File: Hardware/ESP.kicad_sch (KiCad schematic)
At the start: 30 parts, among them J2 USB_C_Receptacle_USB2.0_16P, SW1 RESET, SW2 BOOT, U1 ESP32-C6-MINI-1/U, U2 TPS2115ADRBR, U8 LT1963AEST-3.3#TRPBF

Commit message: revB updates
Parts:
- removed C18: 0.1u, Capacitor_SMD:C_0603_1608Metric, symbol Device:C
- removed R15, R22, R23: 10k, Resistor_SMD:R_0603_1608Metric, symbol Device:R_US
- removed SW1: RESET, UTSVT_Special:SW_SPST_B3SL-1002P, symbol Switch:SW_MEC_5G
- removed SW2: BOOT, UTSVT_Special:SW_CJS-1200TA, symbol Switch:SW_SPDT
- added R1: 10k, Resistor_SMD:R_0603_1608Metric, symbol Device:R_US
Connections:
- net BOOT_SWITCH is gone; now on net BOOT: U1.23 (GPIO9)
- net +3.3V_ESP: now also R7.1, TP47.1, R1.1
- net +3.3V_USB: no longer R7.1, TP47.1
- net BOOT: no longer U1.22 (GPIO8)
- new net: R1.2, U1.22 (GPIO8)

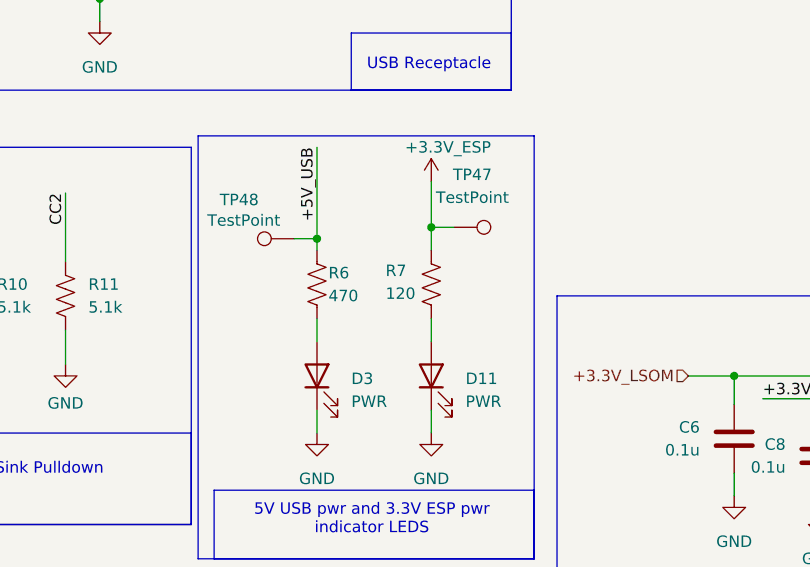
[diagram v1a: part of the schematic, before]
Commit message: Schematic polishes, layout WIP
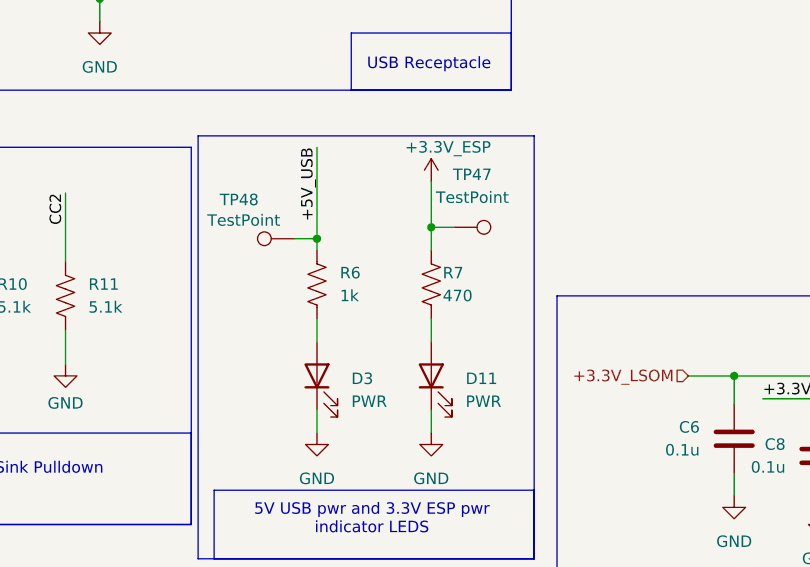
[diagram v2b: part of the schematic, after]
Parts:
- R6: value 470 -> 1k; P/N CRCW1206470RFKEA -> CRCW06031K00FKEI
- R7: value 120 -> 470; P/N CRCW0603120RFKEC -> CRCW1206470RFKEA
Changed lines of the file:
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@@
+	)
+	(symbol
+		(lib_id "Device:R_US")
+		(at 73.66 105.41 0)
+		(unit 1)
+		(exclude_from_sim no)
+		(in_bom yes)
+		(on_board yes)
+		(dnp no)
+		(property "Reference" "R7"
+			(at 74.93 104.14 0)
+			(effects
+				(font
+					(size 1.27 1.27)
+				)
+				(justify left)
+			)
+		)
+		(property "Value" "470"
+			(at 74.93 106.68 0)
+			(effects
+				(font
+					(size 1.27 1.27)
+				)
+				(justify left)
+			)
+		)
+		(property "Footprint" "Resistor_SMD:R_0603_1608Metric"
+			(at 74.676 105.664 90)
+			(effects
+				(font
+					(size 1.27 1.27)
+				)
+				(hide yes)
+			)
+		)
+		(property "Datasheet" "https://www.vishay.com/doc?20035"
+			(at 73.66 105.41 0)
+			(effects
+				(font
+					(size 1.27 1.27)
+				)
+				(hide yes)
+			)
+		)
+		(property "Description" "Resistor, US symbol"
+			(at 73.66 105.41 0)
+			(effects
+				(font
+					(size 1.27 1.27)
+				)
+				(hide yes)
+			)
+		)
+		(property "Manufactuerer" "Vishay "
+			(at 73.66 105.41 0)
+			(effects
+				(font
+					(size 1.27 1.27)
+				)
+				(hide yes)
+			)
+		)
+		(property "P/N" "CRCW1206470RFKEA "
+			(at 73.66 105.41 0)
+			(effects
+				(font
+					(size 1.27 1.27)
+				)
+				(hide yes)
+			)
+		)
+		(pin "2"
+		)
+		(pin "1"
+		)
+		(instances
+			(project "BPS-Leader"
+				(path "/fb37da34-e420-4994-8cc1-079e8c0fa48e/dabc680e-023d-4bcf-9356-bacd091b1cc9"
+					(reference "R7")
+					(unit 1)
+				)
+			)
+		)
 	)
 	(symbol
@@
 	)
 	(symbol
-		(lib_id "Device:R_US")
-		(at 60.96 105.41 0)
-		(unit 1)
-		(exclude_from_sim no)
-		(in_bom yes)
-		(on_board yes)
-		(dnp no)
-		(property "Reference" "R6"
-			(at 62.23 104.14 0)
-			(effects
-				(font
-					(size 1.27 1.27)
-				)
-				(justify left)
-			)
-		)
-		(property "Value" "470"
-			(at 62.23 106.68 0)
-			(effects
-				(font
-					(size 1.27 1.27)
-				)
-				(justify left)
-			)
-		)
-		(property "Footprint" "Resistor_SMD:R_0603_1608Metric"
-			(at 61.976 105.664 90)
-			(effects
-				(font
-					(size 1.27 1.27)
-				)
-				(hide yes)
-			)
-		)
-		(property "Datasheet" "https://www.vishay.com/doc?20035"
-			(at 60.96 105.41 0)
-			(effects
-				(font
-					(size 1.27 1.27)
-				)
-				(hide yes)
-			)
-		)
-		(property "Description" "Resistor, US symbol"
-			(at 60.96 105.41 0)
-			(effects
-				(font
-					(size 1.27 1.27)
-				)
-				(hide yes)
-			)
-		)
-		(property "Manufactuerer" "Vishay "
-			(at 60.96 105.41 0)
-			(effects
-				(font
-					(size 1.27 1.27)
-				)
-				(hide yes)
-			)
-		)
-		(property "P/N" "CRCW1206470RFKEA "
-			(at 60.96 105.41 0)
-			(effects
-				(font
-					(size 1.27 1.27)
-				)
-				(hide yes)
-			)
-		)
-		(pin "2"
-		)
-		(pin "1"
-		)
-		(instances
-			(project "BPS-Leader"
-				(path "/fb37da34-e420-4994-8cc1-079e8c0fa48e/dabc680e-023d-4bcf-9356-bacd091b1cc9"
-					(reference "R6")
-					(unit 1)
-				)
-			)
-		)
-	)
-	(symbol
 		(lib_id "power:+3V3")
 		(at 179.705 115.57 0)
@@
 	)
 	(symbol
-		(lib_id "Device:R_US")
-		(at 73.66 105.41 0)
-		(unit 1)
-		(exclude_from_sim no)
-		(in_bom yes)
-		(on_board yes)
-		(dnp no)
-		(property "Reference" "R7"
-			(at 68.58 103.886 0)
-			(effects
-				(font
-					(size 1.27 1.27)
-				)
-				(justify left)
-			)
-		)
-		(property "Value" "120"
-			(at 68.58 106.426 0)
-			(effects
-				(font
-					(size 1.27 1.27)
-				)
-				(justify left)
-			)
-		)
-		(property "Footprint" "Resistor_SMD:R_0603_1608Metric"
-			(at 74.676 105.664 90)
-			(effects
-				(font
-					(size 1.27 1.27)
-				)
-				(hide yes)
-			)
-		)
-		(property "Datasheet" "https://www.vishay.com/docs/20035/dcrcwe3.pdf"
-			(at 73.66 105.41 0)
-			(effects
-				(font
-					(size 1.27 1.27)
-				)
-				(hide yes)
-			)
-		)
-		(property "Description" "Resistor, US symbol"
-			(at 73.66 105.41 0)
-			(effects
-				(font
-					(size 1.27 1.27)
-				)
-				(hide yes)
-			)
-		)
-		(property "Manufactuerer" "Vishay "
-			(at 73.66 105.41 0)
-			(effects
-				(font
-					(size 1.27 1.27)
-				)
-				(hide yes)
-			)
-		)
-		(property "P/N" "CRCW0603120RFKEC "
-			(at 73.66 105.41 0)
-			(effects
-				(font
-					(size 1.27 1.27)
-				)
-				(hide yes)
-			)
-		)
-		(pin "2"
-		)
-		(pin "1"
-		)
-		(instances
-			(project "BPS-Leader"
-				(path "/fb37da34-e420-4994-8cc1-079e8c0fa48e/dabc680e-023d-4bcf-9356-bacd091b1cc9"
-					(reference "R7")
-					(unit 1)
-				)
-			)
-		)
-	)
-	(symbol
 		(lib_id "power:GND")
 		(at 226.06 90.17 0)
@@
 					(unit 1)
 				)
+			)
+		)
+	)
+	(symbol
+		(lib_id "Device:R_US")
+		(at 60.96 105.41 0)
+		(unit 1)
+		(exclude_from_sim no)
+		(in_bom yes)
+		(on_board yes)
+		(dnp no)
+		(fields_autoplaced yes)
+		(property "Reference" "R6"
+			(at 63.5 104.1399 0)
+			(effects
+				(font
+					(size 1.27 1.27)
+				)
+				(justify left)
+			)
+		)
+		(property "Value" "1k"
+			(at 63.5 106.6799 0)
+			(effects
+				(font
+					(size 1.27 1.27)
+				)
+				(justify left)
+			)
+		)
+		(property "Footprint" "Resistor_SMD:R_0603_1608Metric"
+			(at 61.976 105.664 90)
+			(effects
+				(font
+					(size 1.27 1.27)
+				)
+				(hide yes)
+			)
+		)
+		(property "Datasheet" "https://www.vishay.com/doc?20035"
+			(at 60.96 105.41 0)
+			(effects
+				(font
+					(size 1.27 1.27)
+				)
+				(hide yes)
+			)
+		)
+		(property "Description" "Resistor, US symbol"
+			(at 60.96 105.41 0)
+			(effects
+				(font
+					(size 1.27 1.27)
+				)
+				(hide yes)
+			)
+		)
+		(property "Manufactuerer" "Vishay "
+			(at 60.96 105.41 0)
+			(effects
+				(font
+					(size 1.27 1.27)
+				)
+				(hide yes)
+			)
+		)
+		(property "P/N" "CRCW06031K00FKEI "
+			(at 60.96 105.41 0)
+			(effects
+				(font
+					(size 1.27 1.27)
+				)
+				(hide yes)
+			)
+		)
+		(pin "2"
+		)
+		(pin "1"
+		)
+		(instances
+			(project "BPS-Leader"
+				(path "/fb37da34-e420-4994-8cc1-079e8c0fa48e/dabc680e-023d-4bcf-9356-bacd091b1cc9"
+					(reference "R6")
+					(unit 1)
+				)

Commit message: circuit blocks designed, schematic updated
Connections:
- net IO10: no longer U1.6 (GPIO3/ADC1_CH3)
- net IO12: no longer U1.5 (GPIO2/ADC1_CH2)
- net IO4: no longer U1.16 (MTDO/GPIO7)
- net IO5: no longer U1.15 (MTCK/GPIO6/ADC1_CH6)
- net IO6: no longer U1.13 (GPIO1/ADC1_CH1/XTAL_32K_N)
- net IO7: no longer U1.12 (GPIO0/ADC1_CH0/XTAL_32K_P)
- net IO8: no longer U1.10 (MTDI/GPIO5/ADC1_CH5)
- net IO9: no longer U1.9 (MTMS/GPIO4/ADC1_CH4)
- no-connect marks 7 -> 13
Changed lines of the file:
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@@
-	)
-	(junction
-		(at 254 52.07)
-		(diameter 0)
-		(color 0 0 0 0)
 	)
 	(junction
@@
 	)
 	(no_connect
+		(at 198.12 44.45)
+	)
+	(no_connect
+		(at 198.12 52.07)
+	)
+	(no_connect
 		(at 254 74.93)
 	)
@@
 	)
 	(no_connect
+		(at 198.12 41.91)
+	)
+	(no_connect
+		(at 198.12 39.37)
+	)
+	(no_connect
 		(at 254 69.85)
 	)
@@
 	)
 	(no_connect
+		(at 198.12 36.83)
+	)
+	(no_connect
 		(at 254 72.39)
 	)
+	(no_connect
+		(at 198.12 54.61)
+	)
 	(wire
 		(pts
@@
 	(wire
 		(pts
-			(xy 198.12 59.69) (xy 187.96 59.69)
-		)
-		(stroke
-			(width 0)
-			(type default)
-		)
-	)
-	(wire
-		(pts
 			(xy 33.02 110.49) (xy 33.02 114.3)
 		)
@@
 	(wire
 		(pts
-			(xy 198.12 39.37) (xy 187.96 39.37)
-		)
-		(stroke
-			(width 0)
-			(type default)
-		)
-	)
-	(wire
-		(pts
 			(xy 110.49 118.11) (xy 116.84 118.11)
 		)
@@
 	(wire
 		(pts
-			(xy 198.12 57.15) (xy 187.96 57.15)
-		)
-		(stroke
-			(width 0)
-			(type default)
-		)
-	)
-	(wire
-		(pts
 			(xy 102.235 115.57) (xy 107.315 115.57)
 		)
@@
 	(wire
 		(pts
-			(xy 251.46 52.07) (xy 254 52.07)
-		)
-		(stroke
-			(width 0)
-			(type default)
-		)
-	)
-	(wire
-		(pts
 			(xy 209.55 124.46) (xy 218.44 124.46)
 		)
@@
 	(wire
 		(pts
-			(xy 198.12 36.83) (xy 187.96 36.83)
-		)
-		(stroke
-			(width 0)
-			(type default)
-		)
-	)
-	(wire
-		(pts
 			(xy 162.56 120.65) (xy 169.545 120.65)
 		)
@@
 	(wire
 		(pts
-			(xy 198.12 41.91) (xy 187.96 41.91)
-		)
-		(stroke
-			(width 0)
-			(type default)
-		)
-	)
-	(wire
-		(pts
 			(xy 250.19 127.635) (xy 260.35 127.635)
 		)
@@
 	(wire
 		(pts
-			(xy 198.12 54.61) (xy 187.96 54.61)
-		)
-		(stroke
-			(width 0)
-			(type default)
-		)
-	)
-	(wire
-		(pts
 			(xy 250.19 121.285) (xy 260.35 121.285)
 		)
@@
 	(wire
 		(pts
-			(xy 198.12 52.07) (xy 187.96 52.07)
-		)
-		(stroke
-			(width 0)
-			(type default)
-		)
-	)
-	(wire
-		(pts
 			(xy 250.19 135.255) (xy 260.35 135.255)
 		)
@@
 		(pts
 			(xy 194.31 31.75) (xy 198.12 31.75)
-		)
-		(stroke
-			(width 0)
-			(type default)
-		)
-	)
-	(wire
-		(pts
-			(xy 198.12 44.45) (xy 187.96 44.45)
 		)
 		(stroke
@@
 		)
 	)
-	(label "IO12"
-		(at 187.96 41.91 0)
-		(effects
-			(font
-				(size 1.27 1.27)
-			)
-			(justify left bottom)
-		)
-	)
 	(label "BOOT"
 		(at 264.16 54.61 180)
@@
 		)
 	)
-	(label "IO5"
-		(at 187.96 57.15 0)
-		(effects
-			(font
-				(size 1.27 1.27)
-			)
-			(justify left bottom)
-		)
-	)
 	(label "CC1"
 		(at 58.42 38.1 180)
@@
 		)
 	)
-	(label "IO10"
-		(at 187.96 44.45 0)
-		(effects
-			(font
-				(size 1.27 1.27)
-			)
-			(justify left bottom)
-		)
-	)
 	(label "+5V_USB"
 		(at 24.13 147.32 270)
@@
 		)
 	)
-	(label "IO8"
-		(at 187.96 54.61 0)
-		(effects
-			(font
-				(size 1.27 1.27)
-			)
-			(justify left bottom)
-		)
-	)
 	(label "+5V_USB"
 		(at 60.96 90.17 270)
@@
 		)
 	)
-	(label "IO9"
-		(at 187.96 52.07 0)
-		(effects
-			(font
-				(size 1.27 1.27)
-			)
-			(justify left bottom)
-		)
-	)
 	(label "LED4"
 		(at 264.16 64.77 180)
@@
 		)
 	)
-	(label "IO4"
-		(at 187.96 59.69 0)
-		(effects
-			(font
-				(size 1.27 1.27)
-			)
-			(justify left bottom)
-		)
-	)
 	(label "LED4"
 		(at 209.55 132.08 0)
@@
 		)
 	)
-	(label "IO7"
-		(at 187.96 36.83 0)
-		(effects
-			(font
-				(size 1.27 1.27)
-			)
-			(justify left bottom)
-		)
-	)
-	(label "IO6"
-		(at 187.96 39.37 0)
-		(effects
-			(font
-				(size 1.27 1.27)
-			)
-			(justify left bottom)
-		)
-	)

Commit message: intial layout design
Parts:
- renumbered C8 to C12, C12 to C8
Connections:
- no-connect marks 13 -> 15
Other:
- sheet Buttons_LEDs_IO ports: added none; removed IO10, IO12, IO4, IO5, IO6, IO7, IO8, IO9
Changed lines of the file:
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@@
 	)
 	(junction
-		(at 96.52 33.02)
+		(at 54.61 48.26)
 		(diameter 0)
 		(color 0 0 0 0)
 	)
 	(junction
-		(at 54.61 48.26)
+		(at 125.73 33.02)
 		(diameter 0)
 		(color 0 0 0 0)
 	)
 	(junction
-		(at 125.73 33.02)
+		(at 96.52 33.02)
 		(diameter 0)
 		(color 0 0 0 0)
@@
 	)
 	(no_connect
+		(at 198.12 59.69)
+	)
+	(no_connect
 		(at 52.07 60.96)
 	)
@@
 	)
 	(no_connect
+		(at 198.12 57.15)
+	)
+	(no_connect
 		(at 254 72.39)
 	)
@@
 	(wire
 		(pts
+			(xy 96.52 33.02) (xy 101.6 33.02)
+		)
+		(stroke
+			(width 0)
+			(type default)
+		)
+	)
+	(wire
+		(pts
 			(xy 96.52 44.45) (xy 111.76 44.45)
 		)
@@
 	(wire
 		(pts
-			(xy 96.52 33.02) (xy 101.6 33.02)
-		)
-		(stroke
-			(width 0)
-			(type default)
-		)
-	)
-	(wire
-		(pts
 			(xy 126.365 146.05) (xy 126.365 139.7)
 		)
@@
 	(wire
 		(pts
-			(xy 250.19 127.635) (xy 260.35 127.635)
-		)
-		(stroke
-			(width 0)
-			(type default)
-		)
-	)
-	(wire
-		(pts
 			(xy 22.86 95.25) (xy 22.86 102.87)
 		)
@@
 	(wire
 		(pts
-			(xy 250.19 118.745) (xy 260.35 118.745)
-		)
-		(stroke
-			(width 0)
-			(type default)
-		)
-	)
-	(wire
-		(pts
-			(xy 250.19 121.285) (xy 260.35 121.285)
-		)
-		(stroke
-			(width 0)
-			(type default)
-		)
-	)
-	(wire
-		(pts
 			(xy 86.36 33.02) (xy 96.52 33.02)
 		)
@@
 	(wire
 		(pts
-			(xy 250.19 130.175) (xy 260.35 130.175)
-		)
-		(stroke
-			(width 0)
-			(type default)
-		)
-	)
-	(wire
-		(pts
 			(xy 254 31.75) (xy 257.81 31.75)
 		)
@@
 	(wire
 		(pts
-			(xy 250.19 123.825) (xy 260.35 123.825)
-		)
-		(stroke
-			(width 0)
-			(type default)
-		)
-	)
-	(wire
-		(pts
 			(xy 52.07 38.1) (xy 58.42 38.1)
 		)
@@
 	(wire
 		(pts
-			(xy 250.19 135.255) (xy 260.35 135.255)
-		)
-		(stroke
-			(width 0)
-			(type default)
-		)
-	)
-	(wire
-		(pts
-			(xy 250.19 116.205) (xy 260.35 116.205)
-		)
-		(stroke
-			(width 0)
-			(type default)
-		)
-	)
-	(wire
-		(pts
 			(xy 254 62.23) (xy 264.16 62.23)
 		)
@@
 	(wire
 		(pts
-			(xy 250.19 113.665) (xy 260.35 113.665)
-		)
-		(stroke
-			(width 0)
-			(type default)
-		)
-	)
-	(wire
-		(pts
 			(xy 194.31 31.75) (xy 198.12 31.75)
 		)
@@
 		)
 	)
-	(label "IO5"
-		(at 260.35 113.665 180)
-		(effects
-			(font
-				(size 1.27 1.27)
-			)
-			(justify right bottom)
-		)
-	)
 	(label "+5V_USB"
 		(at 77.47 33.02 180)
@@
 		)
 	)
-	(label "IO12"
-		(at 260.35 135.255 180)
-		(effects
-			(font
-				(size 1.27 1.27)
-			)
-			(justify right bottom)
-		)
-	)
 	(label "VBUSB"
 		(at 52.07 33.02 0)
@@
 		)
 	)
-	(label "IO8"
-		(at 260.35 121.285 180)
-		(effects
-			(font
-				(size 1.27 1.27)
-			)
-			(justify right bottom)
-		)
-	)
 	(label "LED1"
 		(at 209.55 124.46 0)
@@
 		)
 	)
-	(label "IO10"
-		(at 260.35 130.175 180)
-		(effects
-			(font
-				(size 1.27 1.27)
-			)
-			(justify right bottom)
-		)
-	)
 	(label "+3.3V_USB"
 		(at 138.43 33.02 180)
@@
 		)
 	)
-	(label "IO4"
-		(at 260.35 123.825 180)
-		(effects
-			(font
-				(size 1.27 1.27)
-			)
-			(justify right bottom)
-		)
-	)
 	(label "+5V_USB"
 		(at 60.96 90.17 270)
@@
 		)
 	)
-	(label "IO6"
-		(at 260.35 116.205 180)
-		(effects
-			(font
-				(size 1.27 1.27)
-			)
-			(justify right bottom)
-		)
-	)
 	(label "CC1"
 		(at 22.86 95.25 270)
@@
 		)
 	)
-	(label "IO9"
-		(at 260.35 127.635 180)
-		(effects
-			(font
-				(size 1.27 1.27)
-			)
-			(justify right bottom)
-		)
-	)
 	(label "LED4"
 		(at 264.16 64.77 180)
@@
 		)
 	)
-	(label "IO7"
-		(at 260.35 118.745 180)
-		(effects
-			(font
-				(size 1.27 1.27)
-			)
-			(justify right bottom)
-		)
-	)
 	(label "LED2"
 		(at 209.55 127 0)
@@
 		(on_board yes)
 		(dnp no)
-		(property "Reference" "C12"
+		(property "Reference" "C8"
 			(at 183.515 125.7299 0)
 			(effects
@@
 			(project "BPS-Leader"
 				(path "/fb37da34-e420-4994-8cc1-079e8c0fa48e/dabc680e-023d-4bcf-9356-bacd091b1cc9"
-					(reference "C12")
+					(reference "C8")
 					(unit 1)
 				)
@@
 		(on_board yes)
 		(dnp no)
-		(property "Reference" "C8"
+		(property "Reference" "C12"
 			(at 113.03 123.1899 0)
 			(effects
@@
 			(project "BPS-Leader"
 				(path "/fb37da34-e420-4994-8cc1-079e8c0fa48e/dabc680e-023d-4bcf-9356-bacd091b1cc9"
-					(reference "C8")
+					(reference "C12")
 					(unit 1)
 				)
@@
 			)
 		)
-		(pin "IO5" input
-			(at 250.19 113.665 0)
-			(effects
-				(font
-					(size 1.27 1.27)
-				)
-				(justify right)
-			)
-		)
-		(pin "IO6" input
-			(at 250.19 116.205 0)
-			(effects
-				(font
-					(size 1.27 1.27)
-				)
-				(justify right)
-			)
-		)
-		(pin "IO7" input
-			(at 250.19 118.745 0)
-			(effects
-				(font
-					(size 1.27 1.27)
-				)
-				(justify right)
-			)
-		)
-		(pin "IO8" input
-			(at 250.19 121.285 0)
-			(effects
-				(font
-					(size 1.27 1.27)
-				)
-				(justify right)
-			)
-		)
-		(pin "IO9" input
-			(at 250.19 127.635 0)
-			(effects
-				(font
-					(size 1.27 1.27)
-				)
-				(justify right)
-			)
-		)
-		(pin "IO10" input
-			(at 250.19 130.175 0)
-			(effects
-				(font
-					(size 1.27 1.27)
-				)
-				(justify right)
-			)
-		)
-		(pin "IO12" input
-			(at 250.19 135.255 0)
-			(effects
-				(font
-					(size 1.27 1.27)
-				)
-				(justify right)
-			)
-		)
-		(pin "IO4" input
-			(at 250.19 123.825 0)
-			(effects
-				(font
-					(size 1.27 1.27)
-				)
-				(justify right)
-			)
-		)

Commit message: RevB layout completed
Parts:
- TP47: value TestPoint -> +3.3V_ESP; footprint TestPoint:TestPoint_Pad_1.0x1.0mm -> TestPoint:TestPoint_Keystone_5005-5009_Compact
- TP48: value TestPoint -> +5V_USB; footprint TestPoint:TestPoint_Pad_1.0x1.0mm -> TestPoint:TestPoint_Keystone_5005-5009_Compact
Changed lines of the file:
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@@
 			)
 		)
-		(property "Value" "TestPoint"
+		(property "Value" "+5V_USB"
 			(at 52.832 98.298 90)
 			(effects
@@
 			)
 		)
-		(property "Footprint" "TestPoint:TestPoint_Pad_1.0x1.0mm"
+		(property "Footprint" "TestPoint:TestPoint_Keystone_5005-5009_Compact"
 			(at 58.42 95.25 0)
 			(effects
@@
 			)
 		)
-		(property "Value" "TestPoint"
+		(property "Value" "+3.3V_ESP"
 			(at 78.232 95.758 90)
 			(effects
@@
 			)
 		)
-		(property "Footprint" "TestPoint:TestPoint_Pad_1.0x1.0mm"
+		(property "Footprint" "TestPoint:TestPoint_Keystone_5005-5009_Compact"
 			(at 76.2 93.98 0)
 			(effects
